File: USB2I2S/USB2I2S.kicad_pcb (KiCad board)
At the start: 4 copper layers, 19.1 x 29.2 mm, 8 parts, among them J8 USB_B_Micro, J9 Conn_01x06_Male, U6 CP2615-A01-GM

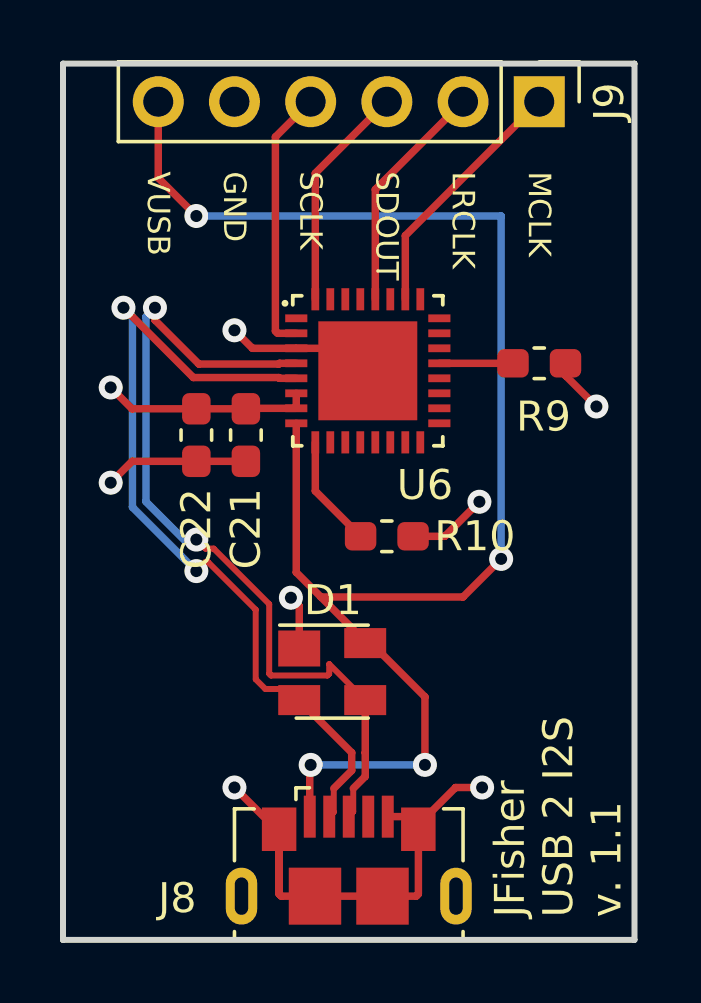
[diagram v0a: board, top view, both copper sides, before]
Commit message: Fixed the VUSB <-> REGIN error causing board not to create Vcc.
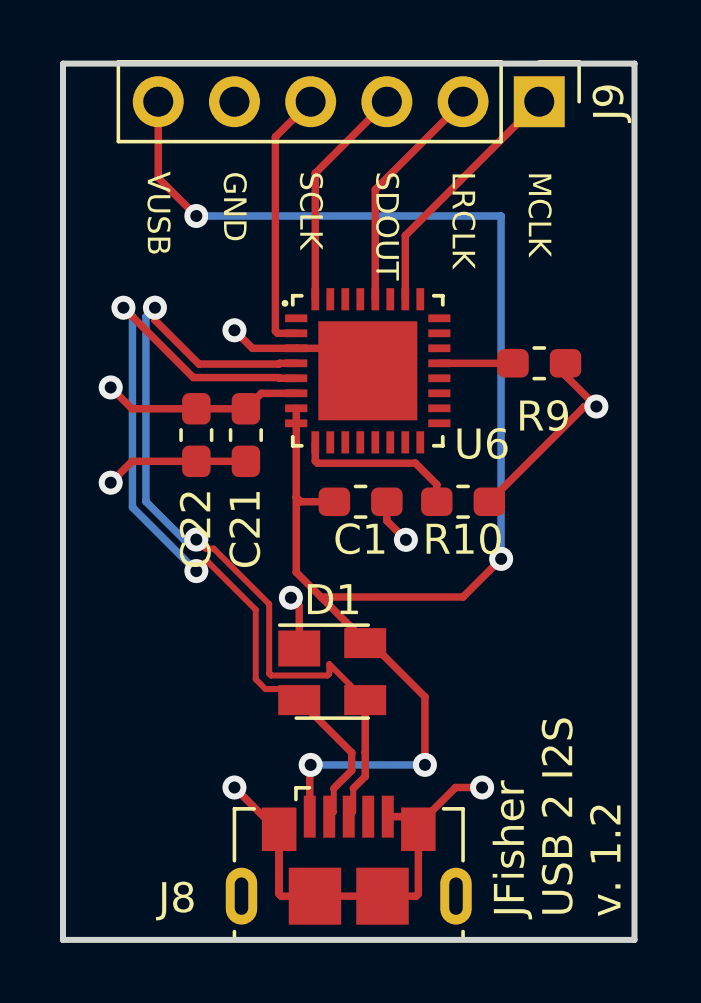
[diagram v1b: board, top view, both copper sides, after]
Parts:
- added C1: 1uF, Capacitor_SMD:C_0603_1608Metric_Pad1.05x0.95mm_HandSolder, F.Cu at (113.4, 126.4)
- moved R10 2.79 mm to (116.8, 126.4)
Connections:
- U6 pad 7: VCC -> VBUS_IN
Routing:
- net VCC: track 11.5 -> 13.4 mm, vias 3 -> 2
- net VBUS_IN: track 51.3 -> 53.1 mm
- net Net-(R10-Pad2): track 3.76 -> 5.57 mm
- net GND: track 28.8 -> 30.4 mm, vias 5 -> 6
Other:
- board text added: "JFisher USB 2 I2S v. 1.2"
- board text removed: "JFisher USB 2 I2S v. 1.1"
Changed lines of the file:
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@@
     (thickness 1.6)
     (drawings 11)
-    (tracks 125)
+    (tracks 133)
     (zones 0)
-    (modules 8)
+    (modules 9)
     (nets 12)
   )
@@
     (add_net VCC)
   )
+  (module Capacitor_SMD:C_0603_1608Metric_Pad1.05x0.95mm_HandSolder (layer F.Cu)
+    (at 113.425 126.365)
+    (descr "Capacitor SMD 0603 (1608 Metric), square (rectangular) end terminal, IPC_7351 nominal with elongated pad for handsoldering. (Body size source: http://www.tortai-tech.com/upload/download/2011102023233369053.pdf), generated with kicad-footprint-generator")
+    (tags "capacitor handsolder")
+    (attr smd)
+    (fp_text reference C1 (at 0 1.27) (layer F.SilkS)
+      (effects (font (size 1 1) (thickness 0.15)))
+    )
+    (fp_text value 1uF (at 0 1.43) (layer F.Fab)
+      (effects (font (size 1 1) (thickness 0.15)))
+    )
+    (fp_text user %R (at 0 0) (layer F.Fab)
+      (effects (font (size 0.4 0.4) (thickness 0.06)))
+    )
+    (fp_line (start 1.65 0.73) (end -1.65 0.73) (layer F.CrtYd) (width 0.05))
+    (fp_line (start 1.65 -0.73) (end 1.65 0.73) (layer F.CrtYd) (width 0.05))
+    (fp_line (start -1.65 -0.73) (end 1.65 -0.73) (layer F.CrtYd) (width 0.05))
+    (fp_line (start -1.65 0.73) (end -1.65 -0.73) (layer F.CrtYd) (width 0.05))
+    (fp_line (start -0.171267 0.51) (end 0.171267 0.51) (layer F.SilkS) (width 0.12))
+    (fp_line (start -0.171267 -0.51) (end 0.171267 -0.51) (layer F.SilkS) (width 0.12))
+    (fp_line (start 0.8 0.4) (end -0.8 0.4) (layer F.Fab) (width 0.1))
+    (fp_line (start 0.8 -0.4) (end 0.8 0.4) (layer F.Fab) (width 0.1))
+    (fp_line (start -0.8 -0.4) (end 0.8 -0.4) (layer F.Fab) (width 0.1))
+    (fp_line (start -0.8 0.4) (end -0.8 -0.4) (layer F.Fab) (width 0.1))
+    (pad 2 smd roundrect (at 0.875 0) (size 1.05 0.95) (layers F.Cu F.Paste F.Mask) (roundrect_rratio 0.25)
+      (net 1 GND))
+    (pad 1 smd roundrect (at -0.875 0) (size 1.05 0.95) (layers F.Cu F.Paste F.Mask) (roundrect_rratio 0.25)
+      (net 2 VBUS_IN))
+    (model ${KISYS3DMOD}/Capacitor_SMD.3dshapes/C_0603_1608Metric.wrl
+      (at (xyz 0 0 0))
+      (scale (xyz 1 1 1))
+      (rotate (xyz 0 0 0))
+    )
+  )
   (module Resistor_SMD:R_0603_1608Metric_Pad1.05x0.95mm_HandSolder (layer F.Cu)
     (at 119.38 121.75 180)
@@
   )
   (module Resistor_SMD:R_0603_1608Metric_Pad1.05x0.95mm_HandSolder (layer F.Cu)
-    (at 114.3 127.5165 180)
+    (at 116.84 126.365 180)
     (descr "Resistor SMD 0603 (1608 Metric), square (rectangular) end terminal, IPC_7351 nominal with elongated pad for handsoldering. (Body size source: http://www.tortai-tech.com/upload/download/2011102023233369053.pdf), generated with kicad-footprint-generator")
     (tags "resistor handsolder")
     (attr smd)
-    (fp_text reference R10 (at -2.935 0 180) (layer F.SilkS)
+    (fp_text reference R10 (at 0 -1.27 180) (layer F.SilkS)
       (effects (font (size 1 1) (thickness 0.15)))
     )
@@
     (clearance 0.08)
     (attr smd)
-    (fp_text reference U6 (at 1.905 3.81) (layer F.SilkS)
+    (fp_text reference U6 (at 3.81 2.46) (layer F.SilkS)
       (effects (font (size 1.0001 1.0001) (thickness 0.05)))
     )
@@
       (net 2 VBUS_IN))
     (pad 7 smd rect (at -2.385 1.25 90) (size 0.26 0.74) (layers F.Cu F.Paste F.Mask)
-      (net 9 VCC))
+      (net 2 VBUS_IN))
     (pad 6 smd rect (at -2.385 0.75 90) (size 0.26 0.74) (layers F.Cu F.Paste F.Mask)
       (net 9 VCC))
@@
     (effects (font (size 0.75 0.75) (thickness 0.1)) (justify left))
   )
-  (gr_text "JFisher\nUSB 2 I2S\nv. 1.1" (at 120.015 140.2165 90) (layer F.SilkS)
+  (gr_text "JFisher\nUSB 2 I2S\nv. 1.2" (at 120.015 140.2165 90) (layer F.SilkS)
     (effects (font (size 1 1) (thickness 0.2)) (justify left))
   )
@@
   (segment (start 111.379 131.2575) (end 111.379 129.84175) (width 0.25) (layer F.Cu) (net 1))
   (segment (start 111.379 129.84175) (end 111.101125 129.563875) (width 0.25) (layer F.Cu) (net 1))
+  (via (at 114.935 127.635) (size 0.8) (drill 0.4) (layers F.Cu B.Cu) (net 1))
+  (segment (start 114.3 126.365) (end 114.3 127) (width 0.25) (layer F.Cu) (net 1))
+  (segment (start 114.3 127) (end 114.935 127.635) (width 0.25) (layer F.Cu) (net 1))
   (segment (start 111.73 136.8615) (end 111.73 135.1665) (width 0.25) (layer F.Cu) (net 2))
   (segment (start 111.73 135.1665) (end 111.76 135.1365) (width 0.25) (layer F.Cu) (net 2))
@@
   (segment (start 115.57 135.1365) (end 115.57 132.8685) (width 0.25) (layer F.Cu) (net 2))
   (segment (start 113.579 131.016444) (end 113.579 131.0775) (width 0.25) (layer F.Cu) (net 2))
-  (segment (start 111.28 123.75) (end 111.28 128.717444) (width 0.25) (layer F.Cu) (net 2))
   (segment (start 106.68 113.03) (end 106.68 115.57) (width 0.25) (layer F.Cu) (net 2))
   (segment (start 106.68 115.57) (end 107.95 116.84) (width 0.25) (layer F.Cu) (net 2))
@@
   (via (at 115.57 135.1365) (size 0.8) (drill 0.4) (layers F.Cu B.Cu) (net 2))
   (via (at 111.76 135.1365) (size 0.8) (drill 0.4) (layers F.Cu B.Cu) (net 2))
+  (segment (start 111.435 126.365) (end 111.28 126.21) (width 0.25) (layer F.Cu) (net 2))
+  (segment (start 112.55 126.365) (end 111.435 126.365) (width 0.25) (layer F.Cu) (net 2))
+  (segment (start 111.28 123.75) (end 111.28 126.21) (width 0.25) (layer F.Cu) (net 2))
+  (segment (start 111.28 126.21) (end 111.28 128.717444) (width 0.25) (layer F.Cu) (net 2))
+  (segment (start 111.28 123.25) (end 111.28 123.75) (width 0.25) (layer F.Cu) (net 2))
   (segment (start 111.915 115.415) (end 111.915 119.615) (width 0.25) (layer F.Cu) (net 3))
   (segment (start 114.3 113.03) (end 111.915 115.415) (width 0.25) (layer F.Cu) (net 3))
@@
   (segment (start 111.76 113.03) (end 110.584999 114.205001) (width 0.25) (layer F.Cu) (net 6))
   (segment (start 116.05 121.75) (end 118.505 121.75) (width 0.25) (layer F.Cu) (net 7))
-  (segment (start 111.915 126.0065) (end 111.915 124.385) (width 0.25) (layer F.Cu) (net 8))
-  (segment (start 113.425 127.5165) (end 111.915 126.0065) (width 0.25) (layer F.Cu) (net 8))
-  (segment (start 111.28 122.75) (end 111.28 123.25) (width 0.25) (layer F.Cu) (net 9))
+  (segment (start 111.915 125.005) (end 111.915 124.385) (width 0.25) (layer F.Cu) (net 8))
+  (segment (start 111.990001 125.080001) (end 111.915 125.005) (width 0.25) (layer F.Cu) (net 8))
+  (segment (start 115.255001 125.080001) (end 111.990001 125.080001) (width 0.25) (layer F.Cu) (net 8))
+  (segment (start 115.965 125.79) (end 115.255001 125.080001) (width 0.25) (layer F.Cu) (net 8))
+  (segment (start 115.965 126.365) (end 115.965 125.79) (width 0.25) (layer F.Cu) (net 8))
   (segment (start 107.95 123.266528) (end 109.601 123.266528) (width 0.25) (layer F.Cu) (net 9))
-  (segment (start 109.617528 123.25) (end 109.601 123.266528) (width 0.25) (layer F.Cu) (net 9))
-  (segment (start 111.28 123.25) (end 109.617528 123.25) (width 0.25) (layer F.Cu) (net 9))
   (via (at 105.095 122.555) (size 0.8) (drill 0.4) (layers F.Cu B.Cu) (net 9))
   (segment (start 107.95 123.266528) (end 105.806528 123.266528) (width 0.25) (layer F.Cu) (net 9))
@@
   (segment (start 120.255 121.75) (end 120.255 122.16) (width 0.25) (layer F.Cu) (net 9))
   (segment (start 120.255 122.16) (end 121.285 123.19) (width 0.25) (layer F.Cu) (net 9))
-  (via (at 117.385 126.365) (size 0.8) (drill 0.4) (layers F.Cu B.Cu) (net 9))
-  (segment (start 115.175 127.5165) (end 116.2335 127.5165) (width 0.25) (layer F.Cu) (net 9))
-  (segment (start 116.2335 127.5165) (end 117.385 126.365) (width 0.25) (layer F.Cu) (net 9))
+  (segment (start 120.89 123.19) (end 121.285 123.19) (width 0.25) (layer F.Cu) (net 9))
+  (segment (start 117.715 126.365) (end 120.89 123.19) (width 0.25) (layer F.Cu) (net 9))
+  (segment (start 110.117528 122.75) (end 111.28 122.75) (width 0.25) (layer F.Cu) (net 9))
+  (segment (start 109.601 123.266528) (end 110.117528 122.75) (width 0.25) (layer F.Cu) (net 9))
   (segment (start 112.529999 136.711501) (end 112.529999 135.921499) (width 0.2) (layer F.Cu) (net 10))
   (segment (start 112.38 136.8615) (end 112.529999 136.711501) (width 0.2) (layer F.Cu) (net 10))
